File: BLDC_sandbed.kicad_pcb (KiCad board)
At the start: 2 copper layers, 60 x 60 mm, 47 parts, among them J1 Conn_01x05_Male, J2 Conn_01x05_Male, Q1 IRF540ZS, Q2 IRF540ZS, Q3 IRF540ZS, Q4 IRF540ZS, Q5 IRF540ZS, Q6 IRF540ZS, U1 IR2104S, U2 IR2104S, U3 IR2104S, U4 LMC6482, U5 NCP1117-12_SOT223, U6 LM3480-3.3

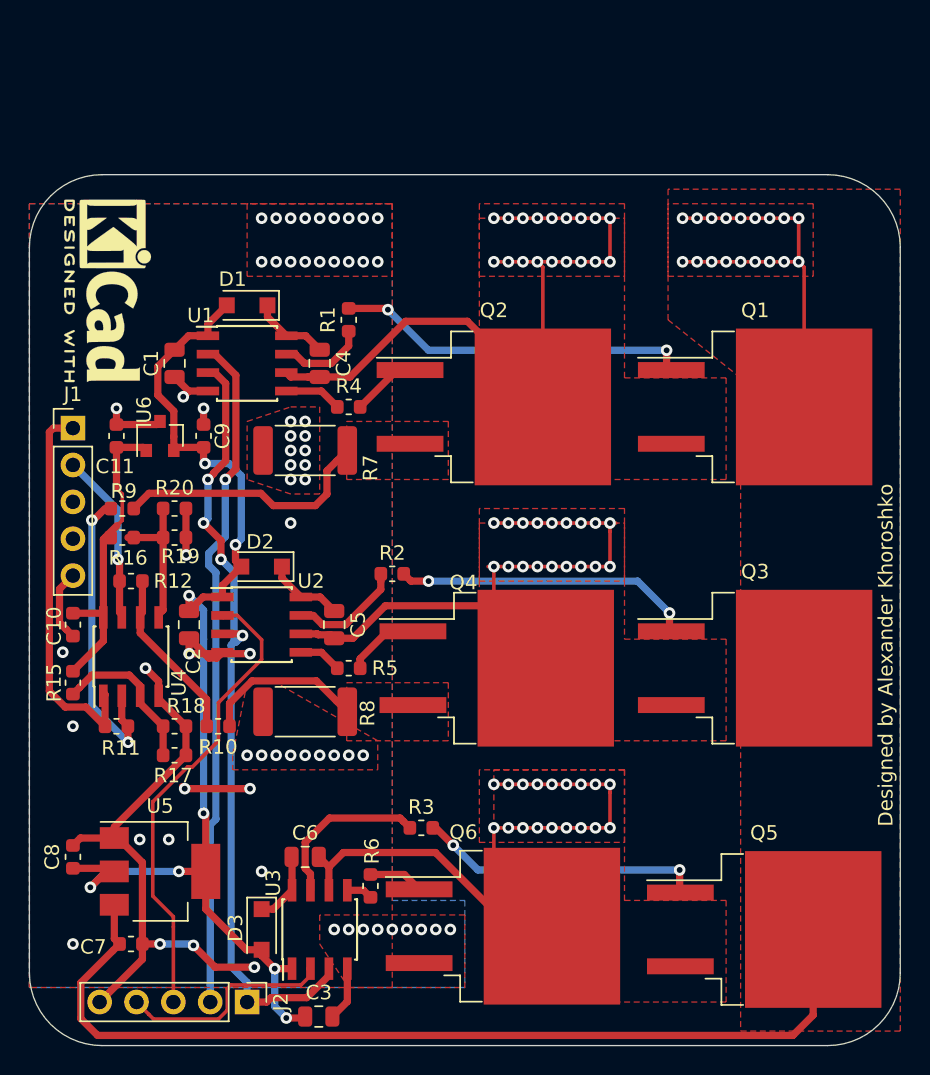
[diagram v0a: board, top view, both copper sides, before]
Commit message: Добавил конденсаторы по питанию
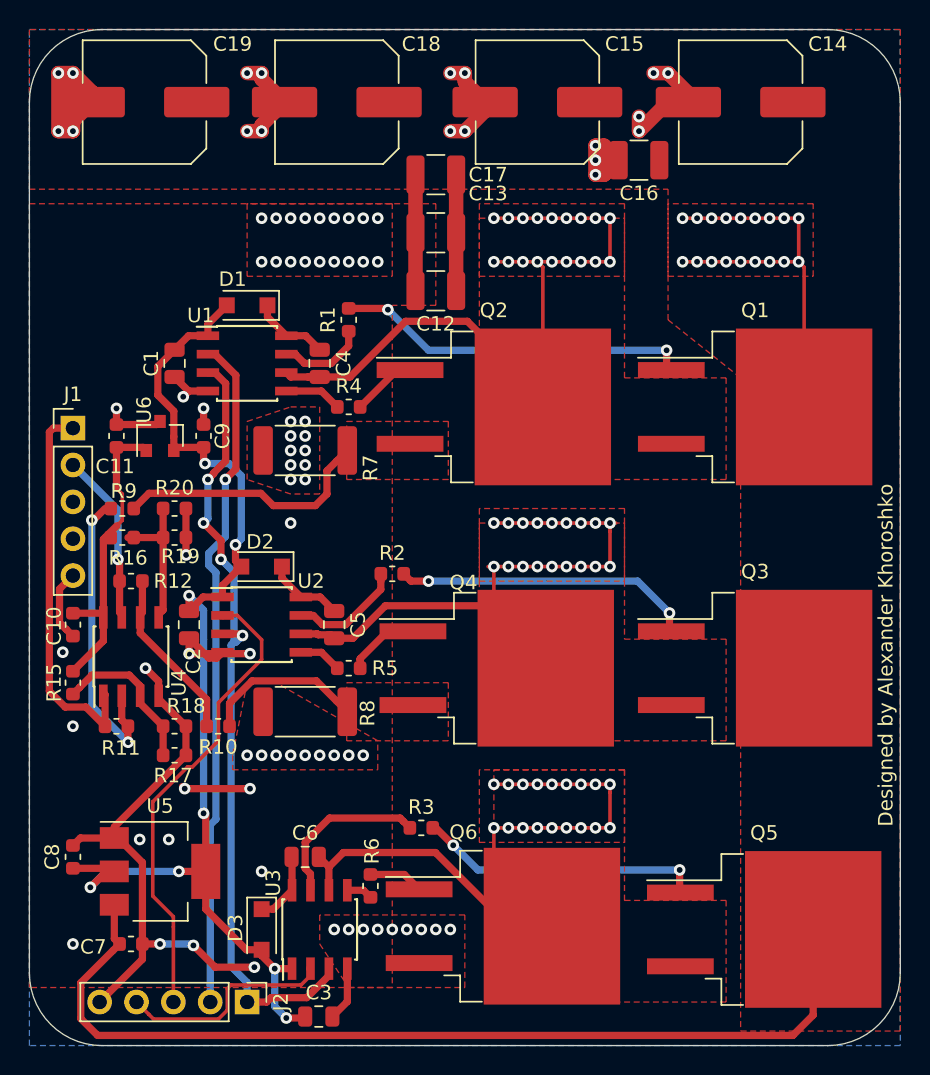
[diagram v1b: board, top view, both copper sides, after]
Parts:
- removed REF**: KiCad-Logo2_5mm_SilkScreen, Symbol:KiCad-Logo2_5mm_SilkScreen
- added C12: 10мк, Capacitor_SMD:C_1210_3225Metric, F.Cu at (58.0, 93.0)
- added C13: 10мк, Capacitor_SMD:C_1210_3225Metric, F.Cu at (58.0, 89.0)
- added C14: 100мк, Capacitor_SMD:C_Elec_8x10.2, F.Cu at (79.0, 80.0)
- added C15: 100мк, Capacitor_SMD:C_Elec_8x10.2, F.Cu at (65.0, 80.0)
- added C16: 10мк, Capacitor_SMD:C_1210_3225Metric, F.Cu at (72.0, 84.0)
- added C17: 10мк, Capacitor_SMD:C_1210_3225Metric, F.Cu at (58.0, 85.0)
- added C18: 100мк, Capacitor_SMD:C_Elec_8x10.2, F.Cu at (51.2, 80.0)
- added C19: 100мк, Capacitor_SMD:C_Elec_8x10.2, F.Cu at (37.9, 80.0)
- U5: value NCP1117-12_SOT223 -> NCP1117ST12T3G
- U6: value LM3480-3.3 -> LM3480IM3-3.3
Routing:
- net GND: track 73.2 -> 127.2 mm, vias 65 -> 84
- net +24V: track 95.7 -> 103.7 mm
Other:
- board size 60 x 60 mm -> 60 x 70 mm

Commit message: небольшие правки
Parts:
- added REF**: KiCad-Logo2_5mm_SilkScreen, Symbol:KiCad-Logo2_5mm_SilkScreen, F.Cu at (34.0, 92.0)
